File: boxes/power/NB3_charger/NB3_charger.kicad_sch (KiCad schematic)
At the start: 40 parts, among them J1 Barrel_Jack_PJ-036AH-SMT-TR, J2 Connector_S4B-PH-SM4-TB(LF)(S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, J3 Conn_01x02_Pin, SW1 SW_SPDT, U1 Voltage_Regulator_AP64501

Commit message: Work on PCBs (v1 and v2)
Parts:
- removed J2: Connector_S4B-PH-SM4-TB(LF)(SN), NB3_charger:Connector_S4B-PH-SM4-TB(LF)(SN), symbol NB3_charger:Connector_S4B-PH-SM4-TB(LF)(SN)
- added H10, H11, H12, H13, H14, H5, H6, H7, H8, H9: MountingHole, MountingHole:MountingHole_2.7mm_M2.5_ISO7380_Pad, symbol Mechanical:MountingHole
- added J2: B4B-PH-K-S, NB3_charger:Connector_B4B-PH-K-S(LF)(SN), symbol NB3_charger:Connector_B4B-PH-K-S(LF)(SN)
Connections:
- net +5V: now also J2.1, J2.2
- net GND: now also J2.3, J2.4
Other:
- moved on the sheet: H1, H2, H3, H4

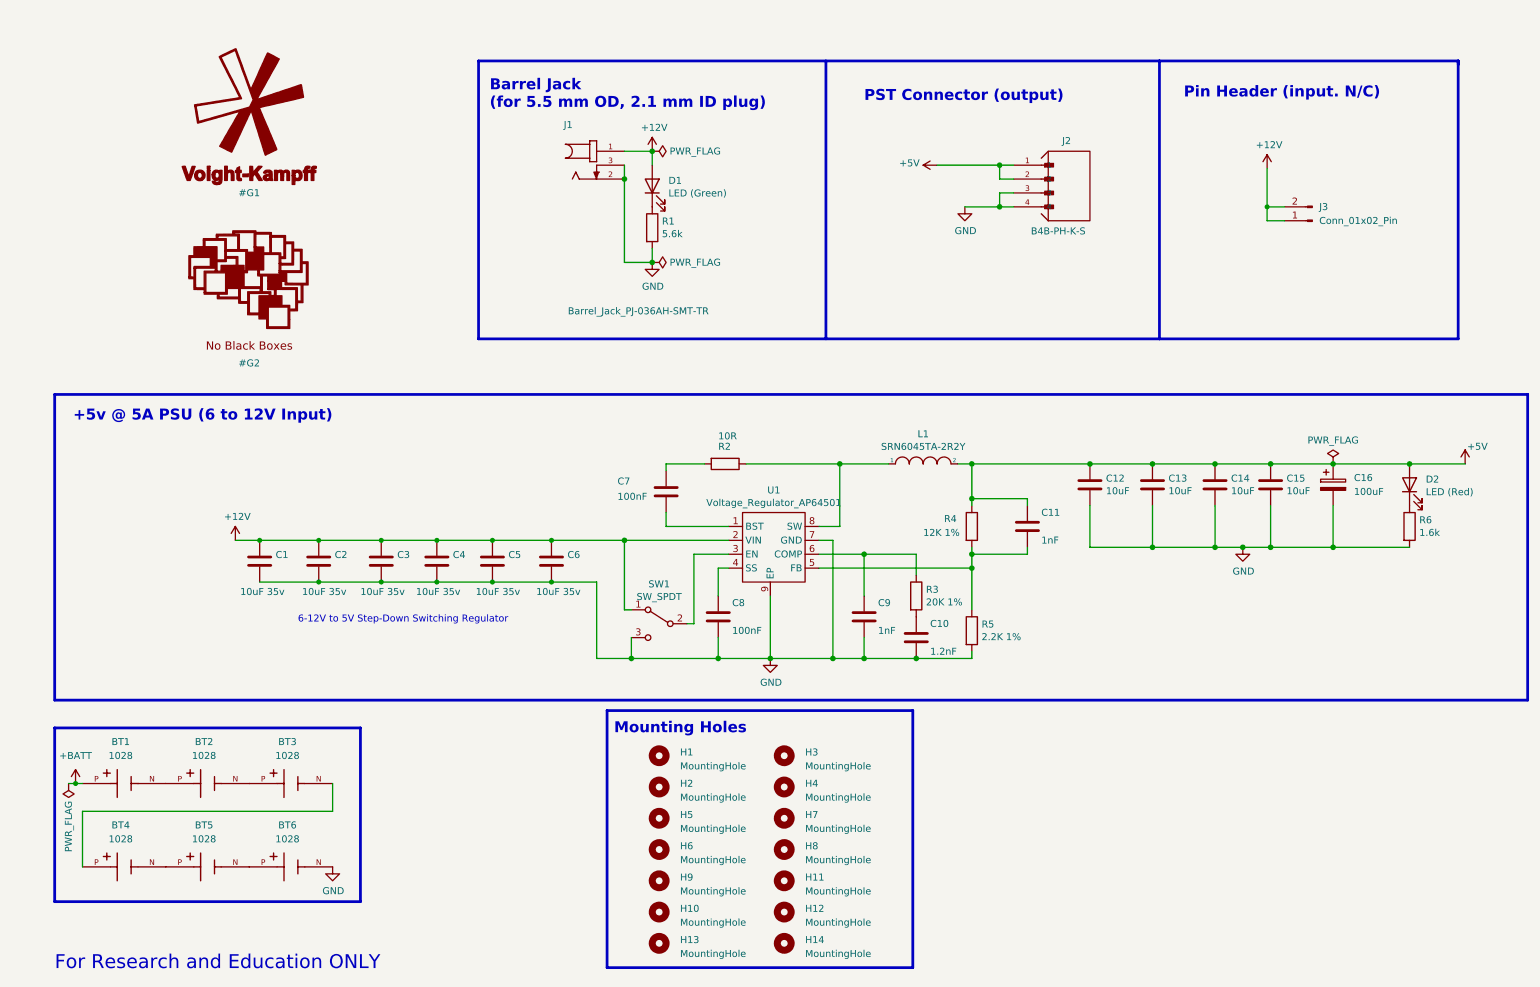
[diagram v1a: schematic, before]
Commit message: PCB tweaks (charger and body)
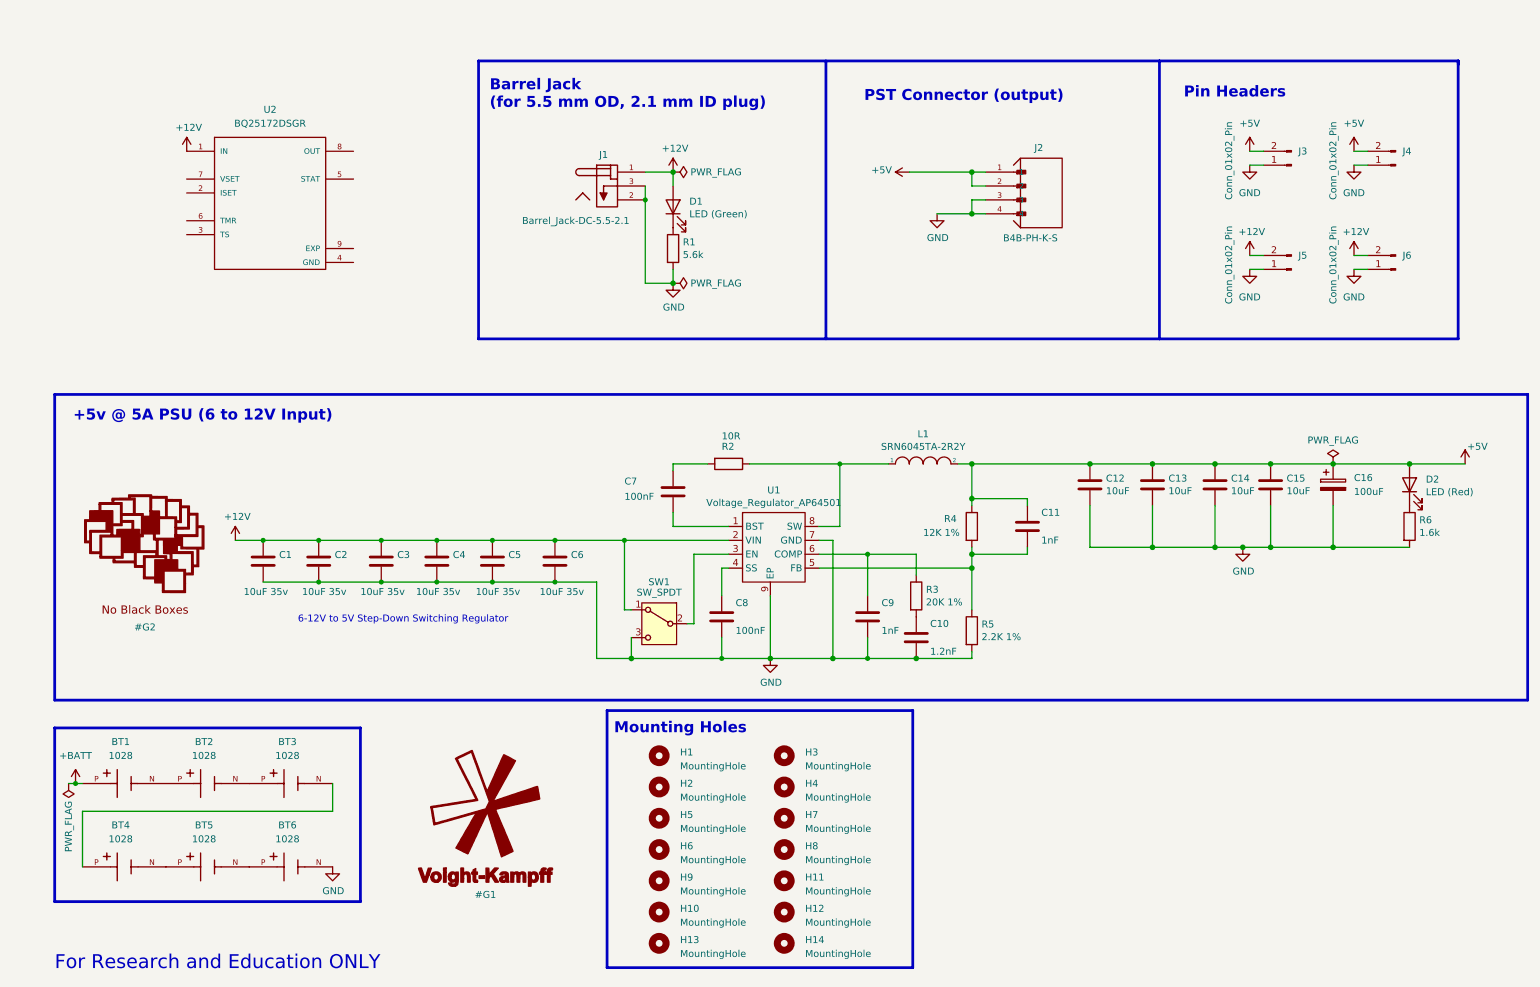
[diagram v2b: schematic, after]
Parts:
- removed J1: Barrel_Jack_PJ-036AH-SMT-TR, NB3_charger:Barrel_Jack_PJ-036AH-SMT-TR, symbol NB3_charger:Barrel_Jack_PJ-036AH-SMT-TR
- added J1: Barrel_Jack-DC-5.5-2.1, NB3_charger:Barrel_Jack_TH_XUNPU_DC-005-A200, symbol NB3_charger:Barrel_Jack_TH_XUNPU_DC-005-A200
- added J4, J5, J6: Conn_01x02_Pin, Connector_PinHeader_2.54mm:PinHeader_1x02_P2.54mm_Vertical, symbol Connector:Conn_01x02_Pin
- added U2: BQ25172DSGR, NiMH_Charger_BQ25172DSGR, symbol NB3_charger:NiMH_Charger_BQ25172DSGR
- J3: footprint Connector_PinHeader_2.54mm:PinHeader_1x02_P2.54mm_Horizontal -> Connector_PinHeader_2.54mm:PinHeader_1x02_P2.54mm_Vertical
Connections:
- net +12V: now also J1.1, J5.2 (Pin_2), J6.2 (Pin_2), U2.1 (IN); no longer J3.1 (Pin_1), J3.2 (Pin_2)
- net +5V: now also J3.2 (Pin_2), J4.2 (Pin_2)
- net GND: now also J3.1 (Pin_1), J1.2, J1.3, J4.1 (Pin_1), J5.1 (Pin_1), J6.1 (Pin_1)
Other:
- note added: "Pin Headers"
- note removed: "Pin Header (input. N/C)"
- moved on the sheet: C1, C6, C7, C8, C9, D1, J2, J3, R1, R2

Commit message: Update NB3 Charger (schematic) with power path
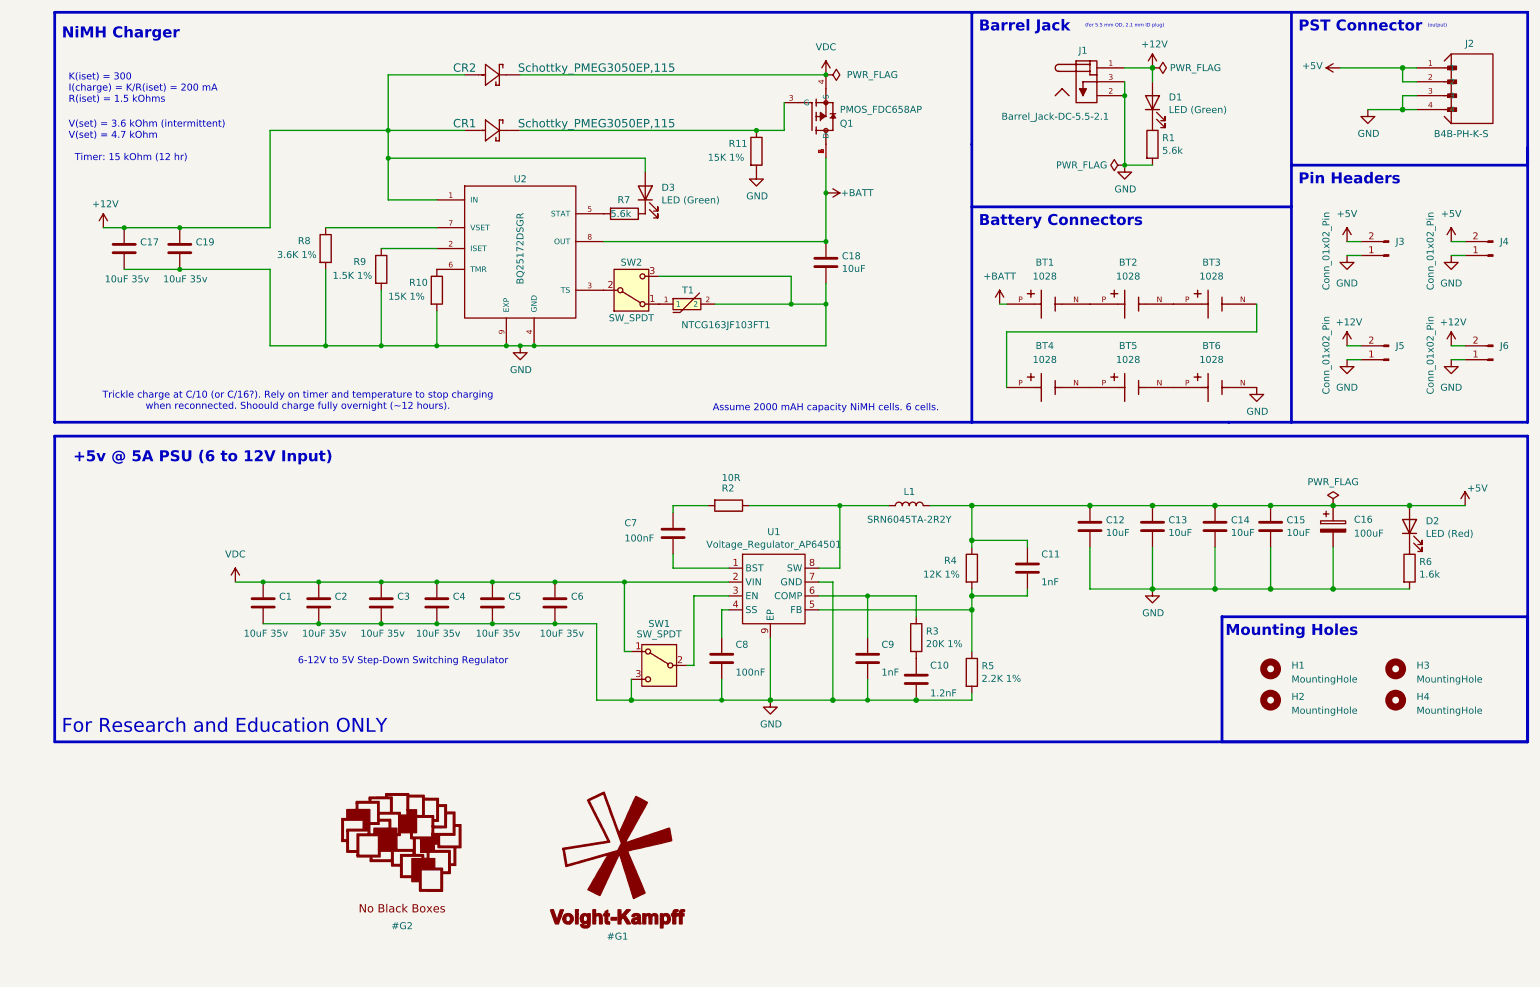
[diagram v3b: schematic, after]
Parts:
- removed H1, H13, H14, H2, H3, H4, H5, H6, H7, H8: MountingHole, MountingHole:MountingHole_2.7mm_M2.5_ISO7380_Pad, symbol Mechanical:MountingHole
- added C17, C19: 10uF 35v, Capacitor_SMD:C_0805_2012Metric, symbol Device:C
- added C18: 10uF, Capacitor_SMD:C_0805_2012Metric, symbol Device:C
- added CR1, CR2: Schottky_PMEG3050EP,115, NB3_charger:Schottky_PMEG3050EP,115, symbol NB3_charger:Schottky_PMEG3050EP,115
- added D3: LED (Green), LED_SMD:LED_0603_1608Metric, symbol Device:LED
- added Q1: PMOS_FDC658AP, NB3_charger:PMOS_SMD_FDC658AP, symbol NB3_charger:PMOS_SMD_FDC658AP
- added R10, R11: 15K 1%, Resistor_SMD:R_0402_1005Metric, symbol Device:R
- added R7: 5.6k, Resistor_SMD:R_0402_1005Metric, symbol Device:R
- added R8: 3.6K 1%, Resistor_SMD:R_0402_1005Metric, symbol Device:R
- added R9: 1.5K 1%, Resistor_SMD:R_0402_1005Metric, symbol Device:R
- added SW2: SW_SPDT, NB3_charger:Switch_SPDT_SMD_Slide_JS102011JCQN, symbol Switch:SW_SPDT
- added T1: NTCG163JF103FT1, NB3_charger:Thermistor_NTC_NTCG163JF103FT1, symbol NB3_charger:Thermistor_NTC_NTCG163JF103FT1
- L1: symbol pspice:INDUCTOR -> Device:L
- U2: footprint NiMH_Charger_BQ25172DSGR -> NB3_charger:NiMH_Charger_BQ25172DSGR
- renumbered H9 to H1, H10 to H2, H11 to H3, H12 to H4
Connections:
- net +12V: now also C17.1, C19.1, CR1.2, CR2.2, D3.2 (A); no longer C1.1, C2.1, C3.1, C4.1, C5.1, C6.1, SW1.1 (A), U1.2 (VIN)
- net +BATT: now also U2.8 (OUT), C18.1, Q1.1 (D), Q1.2 (D), Q1.5 (D), Q1.6 (D)
- net GND: now also U2.4 (GND), U2.9 (EXP), C17.2, C18.2, C19.2, R10.2, R11.2, R8.2, R9.2, SW2.3 (C), T1.2
- net at U2.2 (ISET): now also R9.1
- net at U2.3 (TS): now also SW2.2 (B)
- net at U2.5 (STAT): now also R7.2
- net at U2.6 (TMR): now also R10.1
- net at U2.7 (VSET): now also R8.1
- new net: CR1.1, Q1.3 (G), R11.1
- new net: SW2.1 (A), T1.1
- new net: D3.1 (K), R7.1
- new net VDC: C1.1, C2.1, C3.1, C4.1, C5.1, C6.1, CR2.1, Q1.4 (S), SW1.1 (A), U1.2 (VIN)
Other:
- note added: "(for 5.5 mm OD, 2.1 mm ID plug)"
- note added: "(output)"
- note added: "Assume 2000 mAH capacity NiMH cells. 6 cells."
- note added: "Barrel Jack"
- note added: "Battery Connectors"
- note added: "K(iset) = 300 I(charge) = K/R(iset) = 200 mA R(iset) = 1.5 kOhms"
- note added: "NiMH Charger"
- note added: "PST Connector"
- note added: "Timer: 15 kOhm (12 hr)"
- note added: "Trickle charge at C/10 (or C/16?). Rely on timer and temperature to stop charging when reconnected. Shoould charge fully overnight (~12 hours)."
- note added: "V(set) = 3.6 kOhm (intermittent) V(set) = 4.7 kOhm"
- note removed: "Barrel Jack (for 5.5 mm OD, 2.1 mm ID plug)"
- note removed: "PST Connector (output)"
- moved on the sheet: BT1, BT2, BT3, BT4, BT5, BT6, C1, C10, C11, C12, C13, C14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

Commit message: Update NB3 Charger (schematic notes)
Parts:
- D3: value LED (Green) -> LED (Yellow)
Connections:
- net +12V: no longer J5.2 (Pin_2), J6.2 (Pin_2)
- net VDC: now also J5.2 (Pin_2), J6.2 (Pin_2)
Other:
- note added: "The body diode allows voltage from drain to appear on source, making source more + than gate when external power is disconnected... which opens PMOS."
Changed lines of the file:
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@@
 		)
 	)
+	(text "The body diode allows voltage from drain\nto appear on source, making source more +\nthan gate when external power is\ndisconnected...\nwhich opens PMOS."
+		(exclude_from_sim no)
+		(at 168.91 46.99 0)
+		(effects
+			(font
+				(size 0.635 0.635)
+			)
+		)
+	)
 	(text "NiMH Charger"
 		(exclude_from_sim no)
@@
 	)
 	(symbol
+		(lib_id "power:VDC")
+		(at 269.24 82.55 0)
+		(unit 1)
+		(exclude_from_sim no)
+		(in_bom yes)
+		(on_board yes)
+		(dnp no)
+		(fields_autoplaced yes)
+		(property "Reference" "#PWR012"
+			(at 269.24 86.36 0)
+			(effects
+				(font
+					(size 1.27 1.27)
+				)
+				(hide yes)
+			)
+		)
+		(property "Value" "VDC"
+			(at 269.24 77.47 0)
+			(effects
+				(font
+					(size 1.27 1.27)
+				)
+			)
+		)
+		(property "Footprint" ""
+			(at 269.24 82.55 0)
+			(effects
+				(font
+					(size 1.27 1.27)
+				)
+				(hide yes)
+			)
+		)
+		(property "Datasheet" ""
+			(at 269.24 82.55 0)
+			(effects
+				(font
+					(size 1.27 1.27)
+				)
+				(hide yes)
+			)
+		)
+		(property "Description" "Power symbol creates a global label with name \"VDC\""
+			(at 269.24 82.55 0)
+			(effects
+				(font
+					(size 1.27 1.27)
+				)
+				(hide yes)
+			)
+		)
+		(pin "1"
+		)
+		(instances
+			(project "NB3_charger"
+				(path "/865a6659-88ab-4157-bbc8-8818e83bf79d"
+					(reference "#PWR012")
+					(unit 1)
+				)
+			)
+		)
+	)
+	(symbol
 		(lib_id "Connector:Conn_01x02_Pin")
 		(at 257.81 85.09 180)
@@
 	)
 	(symbol
-		(lib_id "power:+12V")
-		(at 269.24 82.55 0)
-		(unit 1)
-		(exclude_from_sim no)
-		(in_bom yes)
-		(on_board yes)
-		(dnp no)
-		(property "Reference" "#PWR012"
-			(at 269.24 86.36 0)
-			(effects
-				(font
-					(size 1.27 1.27)
-				)
-				(hide yes)
-			)
-		)
-		(property "Value" "+12V"
-			(at 269.6083 78.2256 0)
-			(effects
-				(font
-					(size 1.27 1.27)
-				)
-			)
-		)
-		(property "Footprint" ""
-			(at 269.24 82.55 0)
-			(effects
-				(font
-					(size 1.27 1.27)
-				)
-				(hide yes)
-			)
-		)
-		(property "Datasheet" ""
-			(at 269.24 82.55 0)
-			(effects
-				(font
-					(size 1.27 1.27)
-				)
-				(hide yes)
-			)
-		)
-		(property "Description" "Power symbol creates a global label with name \"+12V\""
-			(at 269.24 82.55 0)
-			(effects
-				(font
-					(size 1.27 1.27)
-				)
-				(hide yes)
-			)
-		)
-		(pin "1"
-		)
-		(instances
-			(project "NB3_charger"
-				(path "/865a6659-88ab-4157-bbc8-8818e83bf79d"
-					(reference "#PWR012")
-					(unit 1)
-				)
-			)
-		)
-	)
-	(symbol
 		(lib_id "Device:R")
 		(at 83.82 72.39 0)
@@
 		)
 		(property "Value" "15K 1%"
-			(at 74.93 73.533 0)
+			(at 81.28 80.01 90)
 			(effects
 				(font
@@
 		)
 		(property "Value" "3.6K 1%"
-			(at 54.61 65.913 0)
+			(at 60.96 73.66 90)
 			(effects
 				(font
@@
 	)
 	(symbol
-		(lib_id "power:+12V")
-		(at 250.19 82.55 0)
-		(unit 1)
-		(exclude_from_sim no)
-		(in_bom yes)
-		(on_board yes)
-		(dnp no)
-		(property "Reference" "#PWR09"
-			(at 250.19 86.36 0)
-			(effects
-				(font
-					(size 1.27 1.27)
-				)
-				(hide yes)
-			)
-		)
-		(property "Value" "+12V"
-			(at 250.5583 78.2256 0)
-			(effects
-				(font
-					(size 1.27 1.27)
-				)
-			)
-		)
-		(property "Footprint" ""
-			(at 250.19 82.55 0)
-			(effects
-				(font
-					(size 1.27 1.27)
-				)
-				(hide yes)
-			)
-		)
-		(property "Datasheet" ""
-			(at 250.19 82.55 0)
-			(effects
-				(font
-					(size 1.27 1.27)
-				)
-				(hide yes)
-			)
-		)
-		(property "Description" "Power symbol creates a global label with name \"+12V\""
-			(at 250.19 82.55 0)
-			(effects
-				(font
-					(size 1.27 1.27)
-				)
-				(hide yes)
-			)
-		)
-		(pin "1"
-		)
-		(instances
-			(project "NB3_charger"
-				(path "/865a6659-88ab-4157-bbc8-8818e83bf79d"
-					(reference "#PWR09")
-					(unit 1)
-				)
-			)
-		)
-	)
-	(symbol
 		(lib_id "NB3_charger:AA_Battery_Holder_1028")
 		(at 210.82 74.93 0)
@@
 		)
 		(property "Value" "1.5K 1%"
-			(at 64.77 69.723 0)
+			(at 71.12 77.47 90)
 			(effects
 				(font
@@
 			)
 		)
-		(property "Value" "LED (Green)"
+		(property "Value" "LED (Yellow)"
 			(at 124.8918 55.9308 90)
 			(effects
@@
 					(unit 1)
 				)
+			)
+		)
+	)
+	(symbol
+		(lib_id "power:VDC")
+		(at 250.19 82.55 0)
+		(unit 1)
+		(exclude_from_sim no)
+		(in_bom yes)
+		(on_board yes)
+		(dnp no)
+		(fields_autoplaced yes)
+		(property "Reference" "#PWR09"
+			(at 250.19 86.36 0)
+			(effects
+				(font
+					(size 1.27 1.27)
+				)
+				(hide yes)
+			)
+		)
+		(property "Value" "VDC"
+			(at 250.19 77.47 0)
+			(effects
+				(font
+					(size 1.27 1.27)
+				)
+			)
+		)
+		(property "Footprint" ""
+			(at 250.19 82.55 0)
+			(effects
+				(font
+					(size 1.27 1.27)
+				)
+				(hide yes)
+			)
+		)
+		(property "Datasheet" ""
+			(at 250.19 82.55 0)
+			(effects
+				(font
+					(size 1.27 1.27)
+				)
+				(hide yes)
+			)
+		)
+		(property "Description" "Power symbol creates a global label with name \"VDC\""
+			(at 250.19 82.55 0)
+			(effects
+				(font
+					(size 1.27 1.27)
+				)
+				(hide yes)
+			)
+		)
+		(pin "1"
+		)
+		(instances
+			(project "NB3_charger"
+				(path "/865a6659-88ab-4157-bbc8-8818e83bf79d"
+					(reference "#PWR09")
+					(unit 1)
+				)

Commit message: Work on NB3 Charger wiring
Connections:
- net +BATT: now also BT6.P; no longer BT1.P
- net GND: now also BT1.N, SW2.1 (A); no longer BT6.N, SW2.3 (C)
- net at BT3.N: now also BT2.P; no longer BT4.P
- net at BT3.P: now also BT4.N; no longer BT2.N
- net at BT5.P: now also BT6.N; no longer BT4.N
- net at BT5.N: now also BT4.P; no longer BT6.P
- net at T1.1: now also SW2.3 (C); no longer SW2.1 (A)
- new net: BT1.P, BT2.N
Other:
- moved on the sheet: BT1, BT2, BT3, BT4, BT5, BT6, T1
